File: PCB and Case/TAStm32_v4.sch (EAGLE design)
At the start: 55 parts, among them CN1 CA0612KRX7R7BB104, CN2 CA0612KRX7R7BB104, CN3 CA0612KRX7R7BB104, CN4 CA0612KRX7R7BB104, IC1 74HCT3G07DP-Q100H, IC2 74HCT3G07DP-Q100H, IC3 74AVCH4T245PW,118, IC4 74AVCH4T245PW,118, J1 ZX62D-B-5PA8, J10 RJSSE538002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

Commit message: no airwires!
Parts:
- CN1, CN2, CN3, CN4: value CA0612KRX7R7BB104 -> 330pF
- RN1, RN2, RN5: value CTS742C083 -> 47K
- RN4, RN7: value CTS742C083 -> 47R
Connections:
- removed net N$13: IC4.2B1, RN7.3
- removed net N$14: IC4.2B2, RN7.4
- removed net N$2: IC3.1B2, RN3.2
- removed net N$3: IC3.1B1, RN3.1
- net ENABLE_P2D2D3: now also U1.PA7
- net N$16: now also CN1.7, RN4.7; no longer CN1.8, RN4.8
- net N$17: now also CN1.5, RN4.5; no longer CN1.7, RN4.7
- net P1_CLOCK: now also RN4.4; no longer RN4.2
- net P1_D2: now also IC3.1B1, RN3.1
- net P1_D3: now also IC3.1B2, RN3.2
- net P1_LATCH: now also RN4.2; no longer RN4.1
- net P1_VCC: now also RN1.5, RN1.6, RN1.7, RN1.8
- net P2_CLOCK: now also RN5.4; no longer RN5.2
- net P2_D2: now also IC4.2B1, RN5.1, RN7.3; no longer RN5.3
- net P2_D2_3V_OUT: now also U1.PB10
- net P2_D3: now also IC4.2B2, RN7.4
- net P2_LATCH: now also RN5.3; no longer RN5.1
- net P2_VCC: now also RN2.5, RN2.6, RN2.7, RN2.8
- net V+: no longer RN1.6, RN1.7, RN1.8, RN2.5, RN2.6, RN2.7, RN2.8
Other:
- note added: "Debug ports"
- note added: "Expansion/Vis Ports"
- note added: "Input Buffers"
- note added: "Output Buffers"
- note removed: "Debug# ports"
- note removed: "Expansion Ports"
- moved on the sheet: C1, C10, C11, C12, C13, C14, C15, C16, C17, C2, C3, C4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

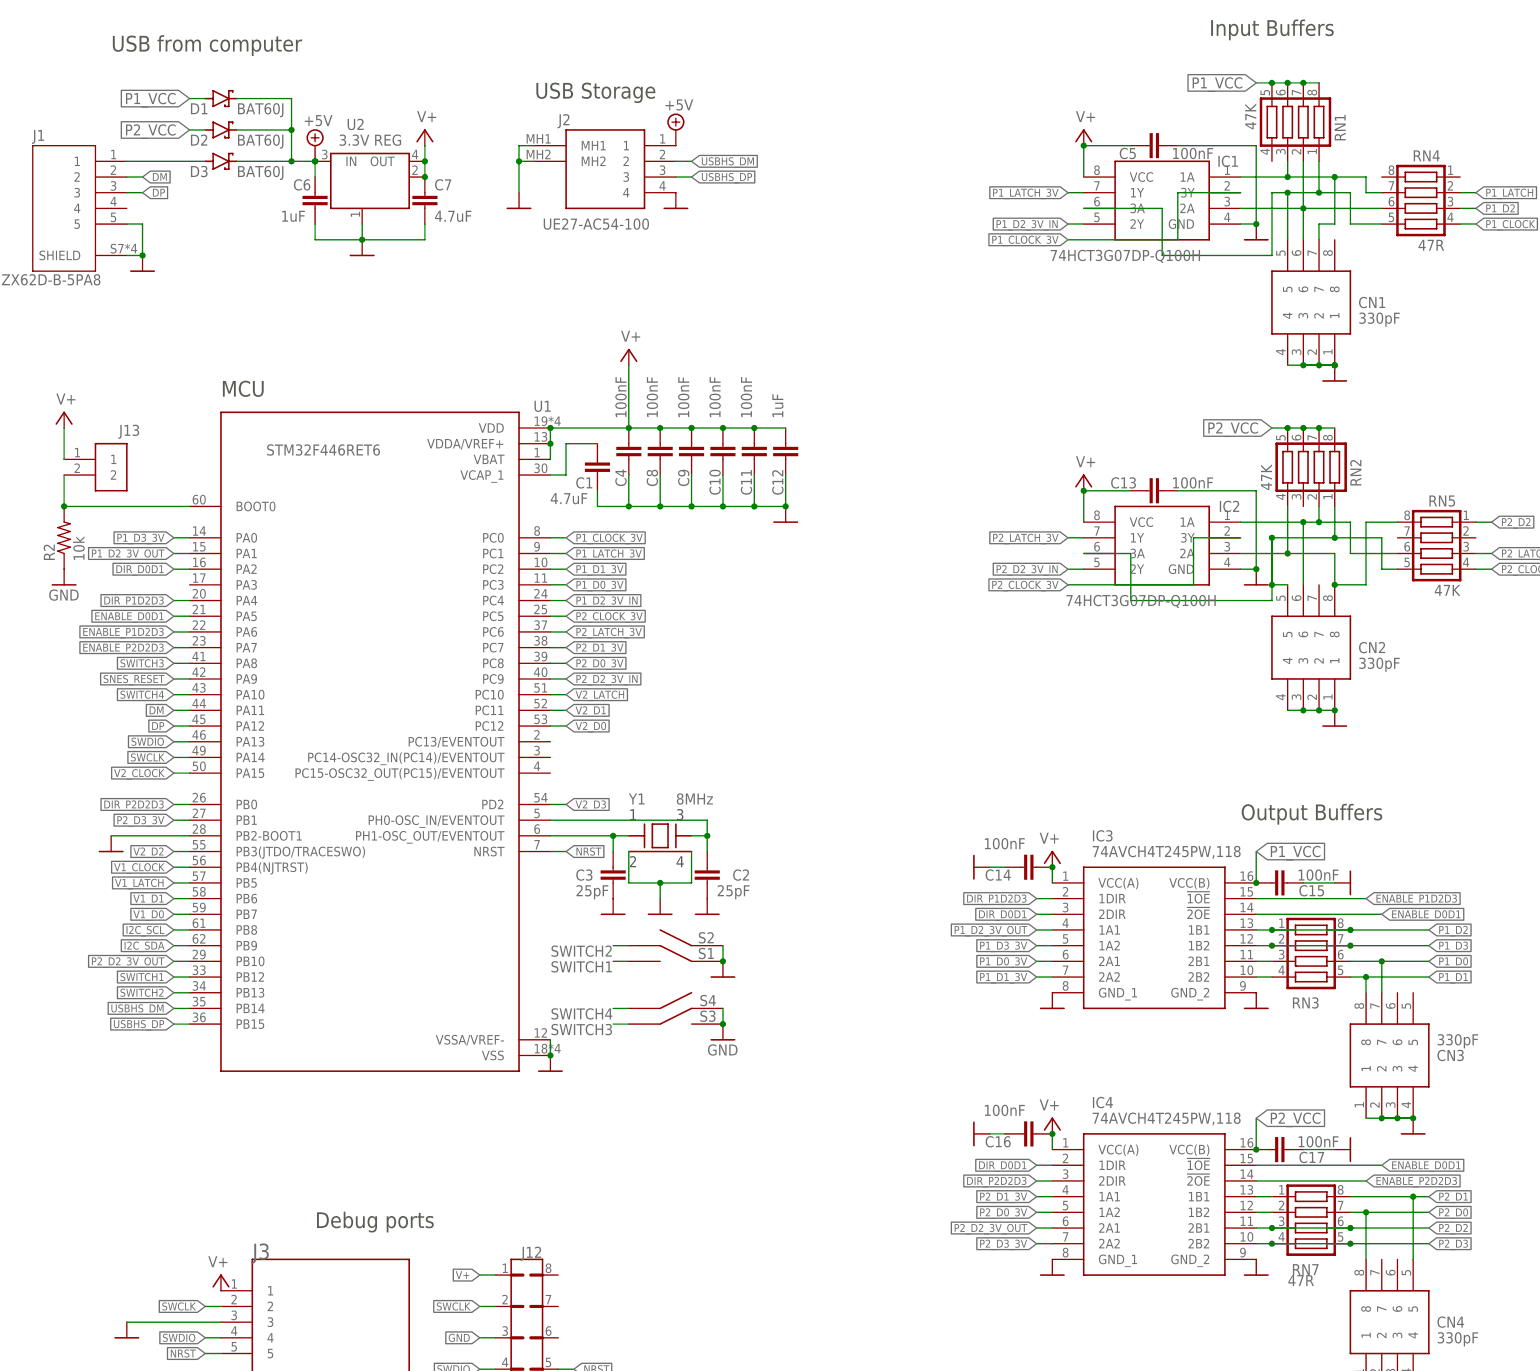
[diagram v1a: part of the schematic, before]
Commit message: more silkscreen cleanup
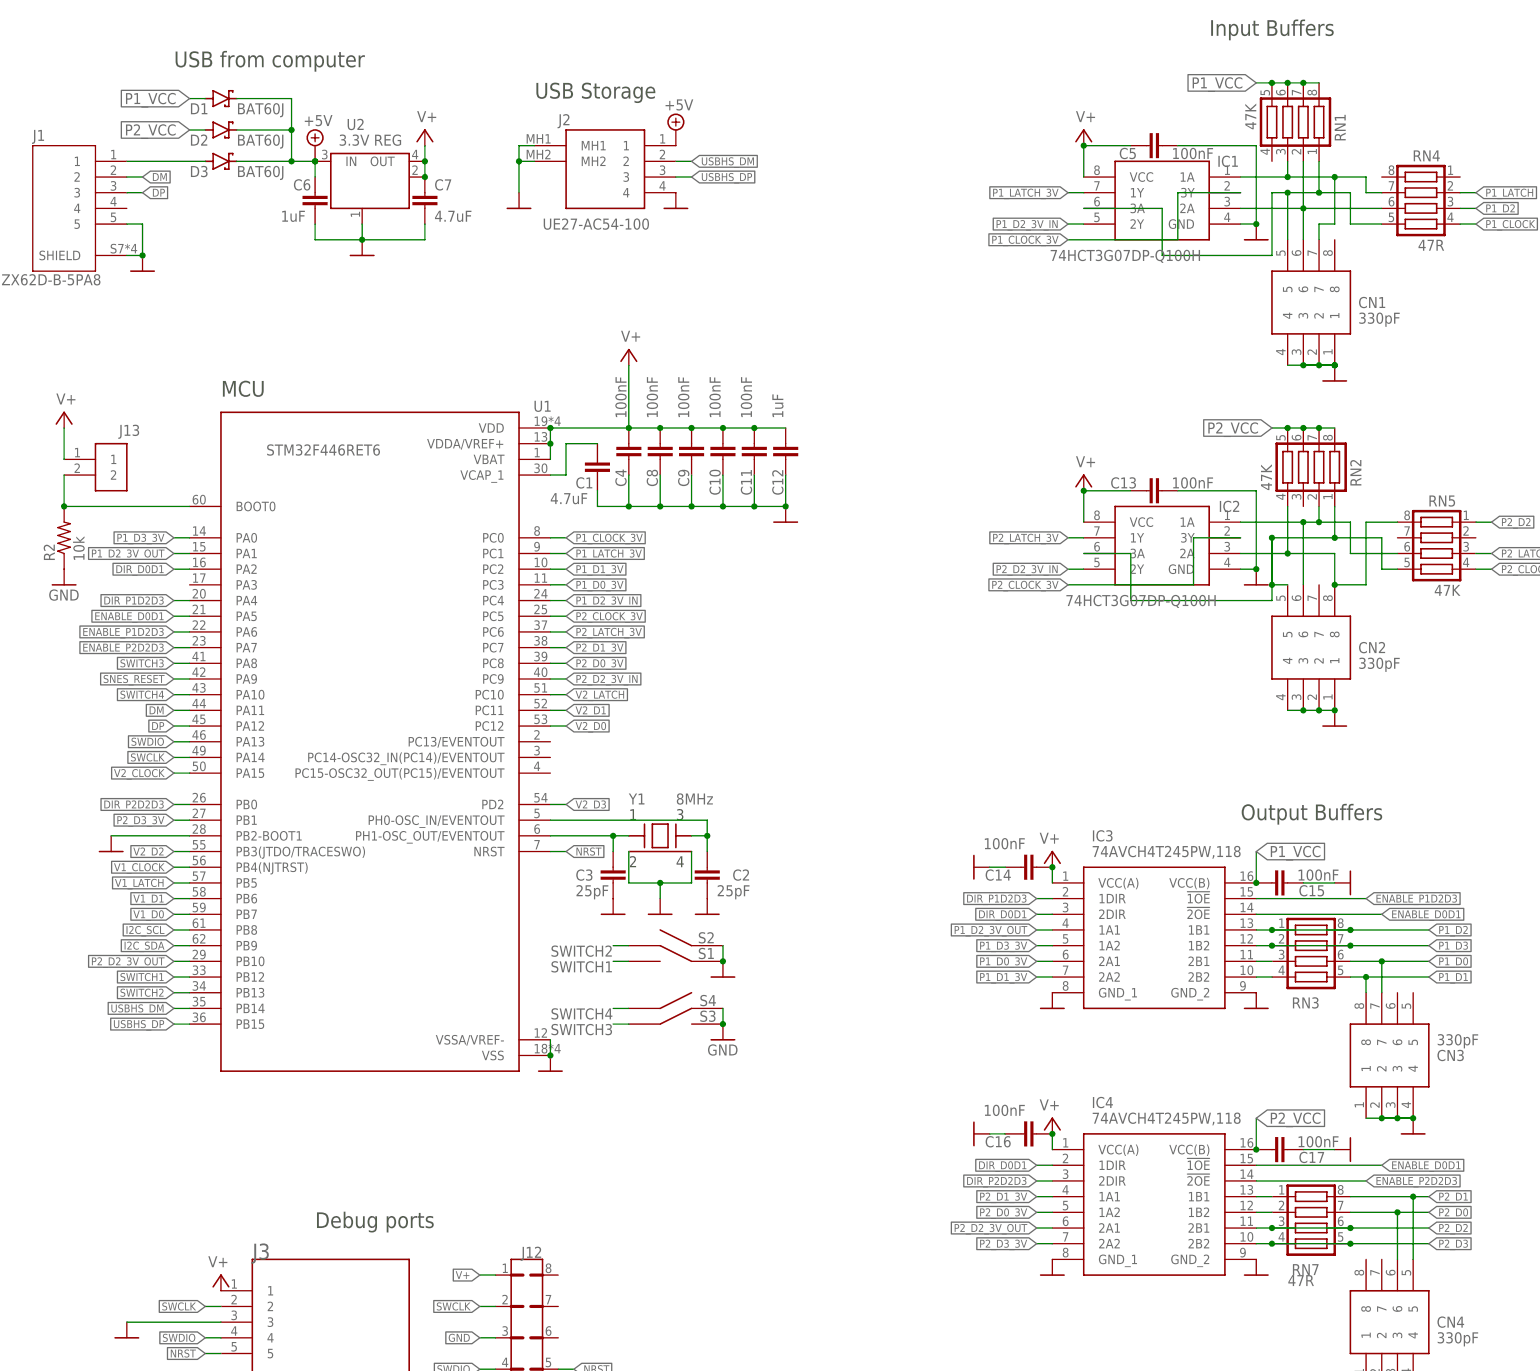
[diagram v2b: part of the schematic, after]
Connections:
- net P2_D0: now also CN4.6; no longer CN4.8
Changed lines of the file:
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@@
 <sheet>
 <plain>
-<text x="33.02" y="243.84" size="2.54" layer="97">USB from computer</text>
+<text x="43.18" y="241.3" size="2.54" layer="97">USB from computer</text>
 <text x="101.6" y="236.22" size="2.54" layer="97">USB Storage</text>
 <text x="50.8" y="187.96" size="2.54" layer="97">MCU</text>
@@
 </segment>
 <segment>
-<wire x1="233.68" y1="55.88" x2="236.22" y2="55.88" width="0.1524" layer="91"/>
 <label x="246.38" y="55.88" size="1.27" layer="95" rot="MR180" xref="yes"/>
 <pinref part="RN7" gate="G$1" pin="7"/>
-<pinref part="CN4" gate="G$1" pin="8"/>
-<wire x1="236.22" y1="55.88" x2="246.38" y2="55.88" width="0.1524" layer="91"/>
-<wire x1="236.22" y1="48.26" x2="236.22" y2="55.88" width="0.1524" layer="91"/>
-<junction x="236.22" y="55.88"/>
-</segment>
-</net>
+<wire x1="233.68" y1="55.88" x2="241.3" y2="55.88" width="0.1524" layer="91"/>
+<pinref part="CN4" gate="G$1" pin="6"/>
+<wire x1="241.3" y1="55.88" x2="246.38" y2="55.88" width="0.1524" layer="91"/>
+<wire x1="241.3" y1="55.88" x2="241.3" y2="48.26" width="0.1524" layer="91"/>
+<junction x="241.3" y="55.88"/>
+</segment>
+</net>

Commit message: spacing out components
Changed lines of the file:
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@@
 <instance part="IC1" gate="G$1" x="215.9" y="223.52" smashed="yes" rot="MR0">
 <attribute name="NAME" x="212.09" y="226.06" size="1.778" layer="95" rot="MR180" align="center-left"/>
-<attribute name="VALUE" x="209.55" y="210.82" size="1.778" layer="96" rot="MR0" align="center-left"/>
+<attribute name="VALUE" x="212.09" y="208.28" size="1.778" layer="96" rot="MR0" align="center-left"/>
 </instance>
 <instance part="IC2" gate="G$1" x="215.9" y="167.64" smashed="yes" rot="MR0">
@@
 <label x="187.96" y="213.36" size="1.27" layer="95" rot="MR0" xref="yes"/>
 <pinref part="IC1" gate="G$1" pin="3Y"/>
-<wire x1="215.9" y1="220.98" x2="205.74" y2="220.98" width="0.1524" layer="91"/>
-<wire x1="205.74" y1="220.98" x2="205.74" y2="213.36" width="0.1524" layer="91"/>
-<wire x1="187.96" y1="213.36" x2="205.74" y2="213.36" width="0.1524" layer="91"/>
+<wire x1="215.9" y1="220.98" x2="203.2" y2="220.98" width="0.1524" layer="91"/>
+<wire x1="203.2" y1="220.98" x2="203.2" y2="213.36" width="0.1524" layer="91"/>
+<wire x1="187.96" y1="213.36" x2="203.2" y2="213.36" width="0.1524" layer="91"/>
 </segment>
 </net>
@@
 <wire x1="223.52" y1="220.98" x2="220.98" y2="220.98" width="0.1524" layer="91"/>
 <wire x1="220.98" y1="220.98" x2="220.98" y2="210.82" width="0.1524" layer="91"/>
-<wire x1="220.98" y1="210.82" x2="203.2" y2="210.82" width="0.1524" layer="91"/>
-<wire x1="203.2" y1="210.82" x2="203.2" y2="218.44" width="0.1524" layer="91"/>
+<wire x1="220.98" y1="210.82" x2="172.72" y2="210.82" width="0.1524" layer="91"/>
+<wire x1="172.72" y1="210.82" x2="172.72" y2="218.44" width="0.1524" layer="91"/>
 <pinref part="IC1" gate="G$1" pin="3A"/>
-<wire x1="203.2" y1="218.44" x2="190.5" y2="218.44" width="0.1524" layer="91"/>
+<wire x1="172.72" y1="218.44" x2="190.5" y2="218.44" width="0.1524" layer="91"/>
 <pinref part="RN1" gate="G$1" pin="1"/>
 <wire x1="228.6" y1="226.06" x2="228.6" y2="220.98" width="0.1524" layer="91"/>

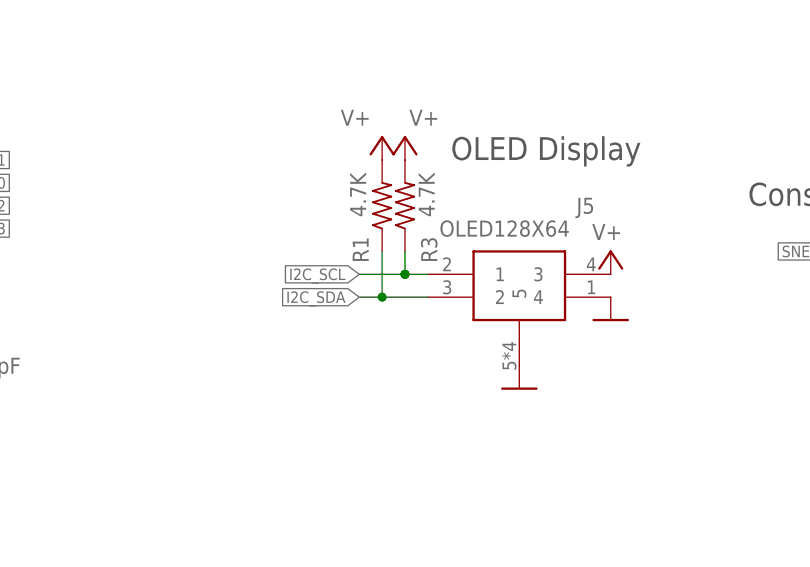
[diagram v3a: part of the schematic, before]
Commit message: ground fill on top
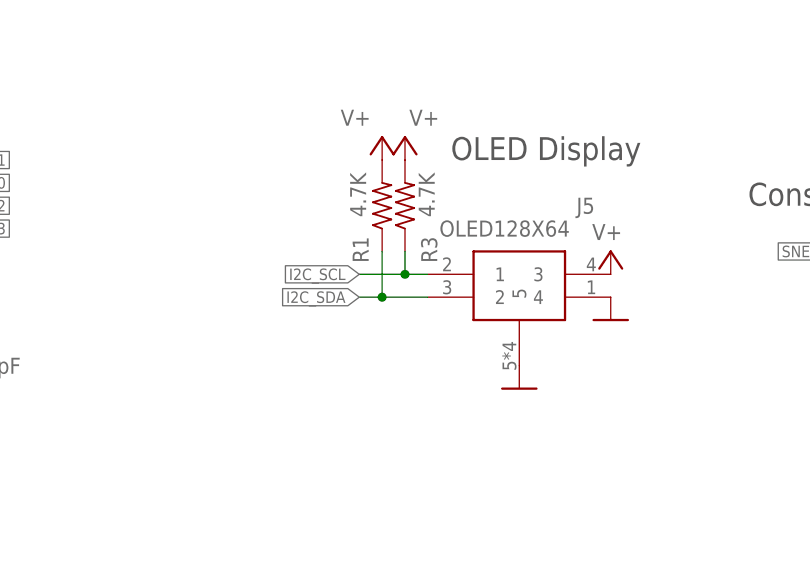
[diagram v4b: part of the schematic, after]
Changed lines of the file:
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@@
 <net name="I2C_SCL" class="0">
 <segment>
+<label x="292.1" y="45.72" size="1.27" layer="95" rot="MR0" xref="yes"/>
 <wire x1="299.72" y1="45.72" x2="297.18" y2="45.72" width="0.1524" layer="91"/>
-<label x="292.1" y="45.72" size="1.27" layer="95" rot="MR0" xref="yes"/>
+<pinref part="J5" gate="G$1" pin="1"/>
 <pinref part="R3" gate="G$1" pin="1"/>
 <wire x1="297.18" y1="45.72" x2="292.1" y2="45.72" width="0.1524" layer="91"/>
 <wire x1="297.18" y1="48.26" x2="297.18" y2="45.72" width="0.1524" layer="91"/>
 <junction x="297.18" y="45.72"/>
-<pinref part="J5" gate="G$1" pin="1"/>
 </segment>
 <segment>
@@
 <net name="I2C_SDA" class="0">
 <segment>
-<wire x1="299.72" y1="43.18" x2="294.64" y2="43.18" width="0.1524" layer="91"/>
 <label x="292.1" y="43.18" size="1.27" layer="95" rot="MR0" xref="yes"/>
 <pinref part="R1" gate="G$1" pin="1"/>
 <wire x1="294.64" y1="43.18" x2="292.1" y2="43.18" width="0.1524" layer="91"/>
 <wire x1="294.64" y1="48.26" x2="294.64" y2="43.18" width="0.1524" layer="91"/>
+<pinref part="J5" gate="G$1" pin="2"/>
+<wire x1="294.64" y1="43.18" x2="299.72" y2="43.18" width="0.1524" layer="91"/>
 <junction x="294.64" y="43.18"/>
-<pinref part="J5" gate="G$1" pin="2"/>
 </segment>
 <segment>
@@
 <wire x1="114.3" y1="114.3" x2="114.3" y2="116.84" width="0.1524" layer="91"/>
 <junction x="114.3" y="116.84"/>
-</segment>
-</net>
-<net name="N$7" class="0">
-<segment>
-<junction x="297.18" y="45.72"/>
 </segment>
 </net>
@@
 </sheet>
 </sheets>
-<errors>
-</errors>
 </schematic>
 </drawing>
